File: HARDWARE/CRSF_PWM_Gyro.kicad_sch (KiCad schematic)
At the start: 3 parts, among them U1 STM32F103T8Ux, U2 TCR2EF33_LMCT

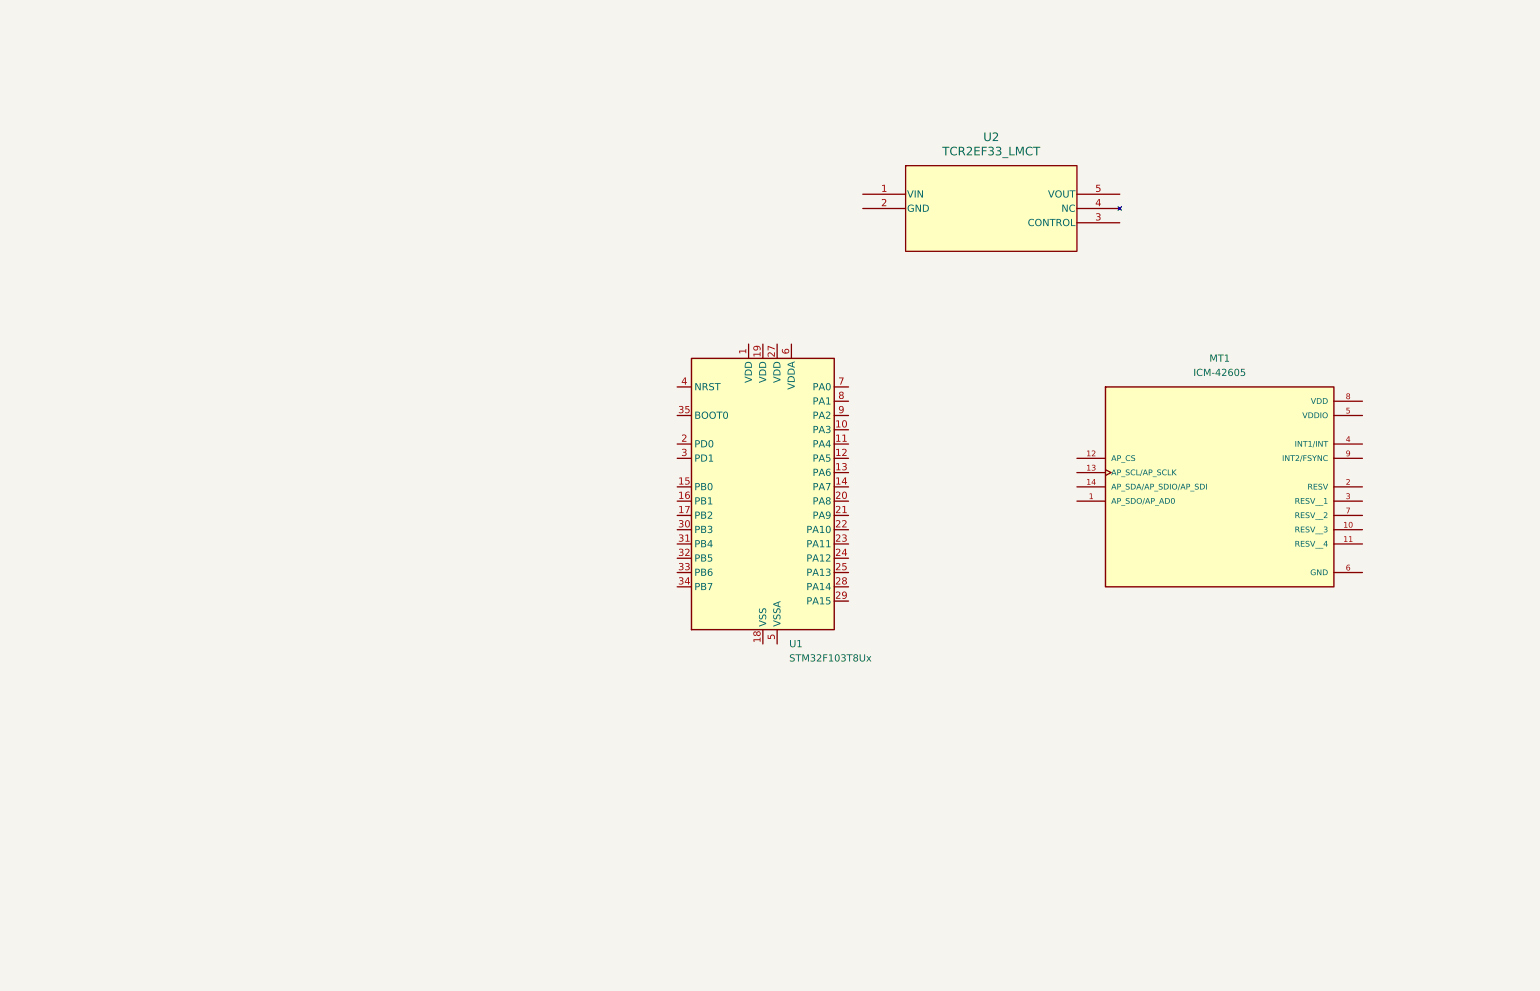
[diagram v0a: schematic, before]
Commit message: Pick different MCU and add USB C connector
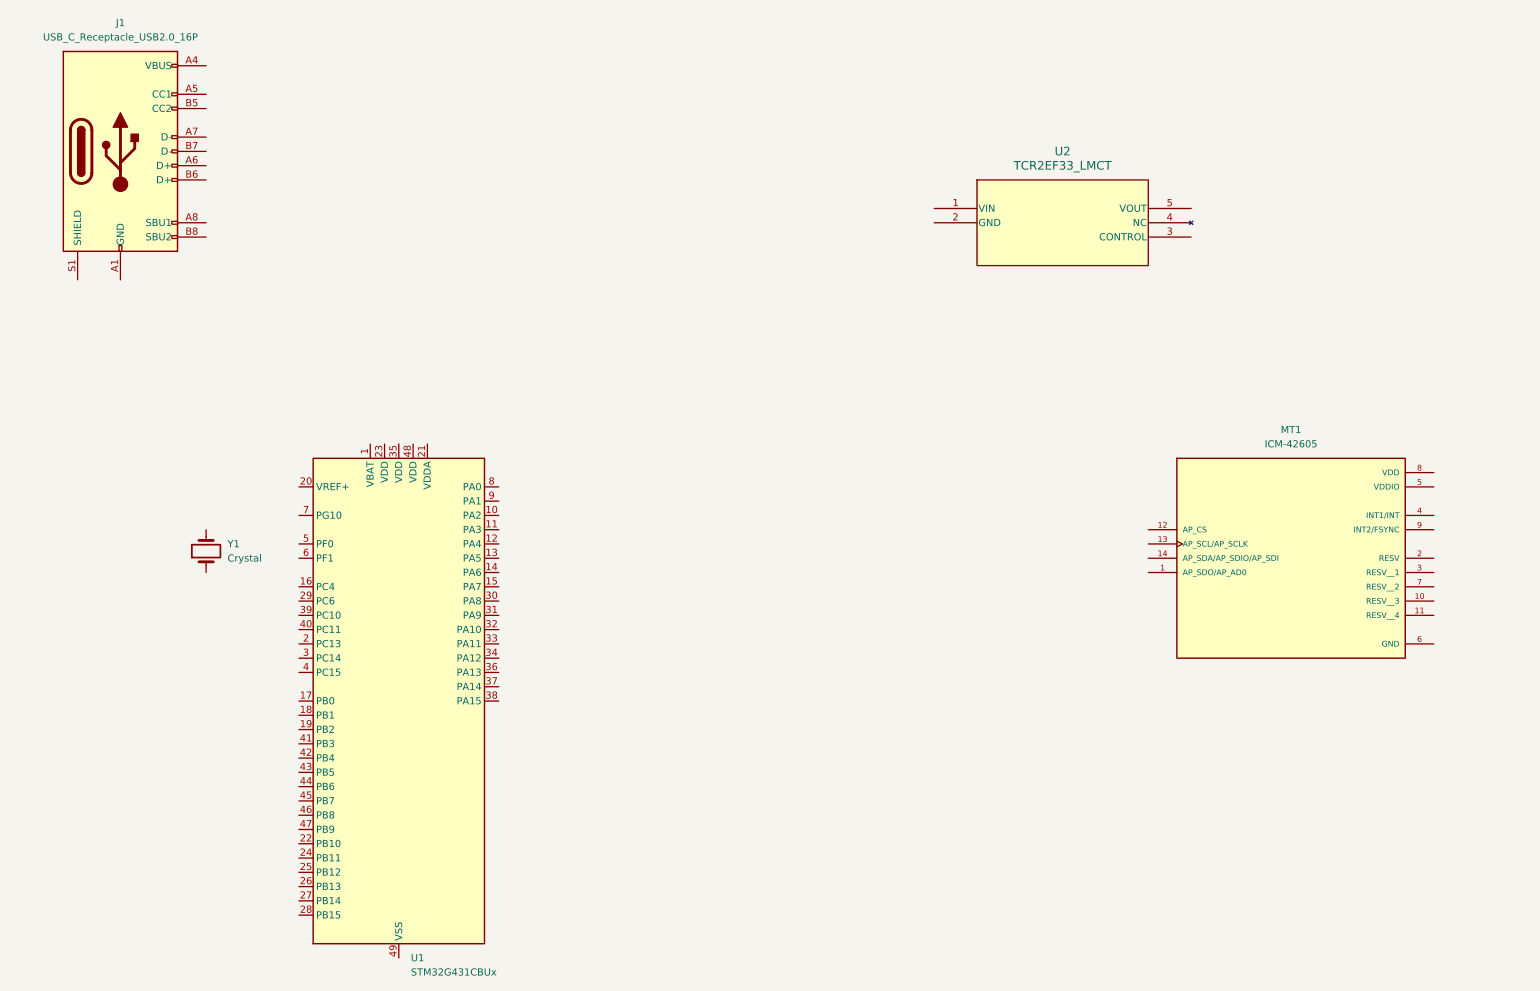
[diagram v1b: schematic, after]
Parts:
- removed U1: STM32F103T8Ux, Package_DFN_QFN:QFN-36-1EP_6x6mm_P0.5mm_EP4.1x4.1mm, symbol MCU_ST_STM32F1:STM32F103T8Ux
- added J1: USB_C_Receptacle_USB2.0_16P, symbol Connector:USB_C_Receptacle_USB2.0_16P
- added U1: STM32G431CBUx, Package_DFN_QFN:QFN-48-1EP_7x7mm_P0.5mm_EP5.6x5.6mm, symbol MCU_ST_STM32G4:STM32G431CBUx
- added Y1: Crystal, symbol Device:Crystal
- MT1: PN ICM-42605 -> (none); Part Number (none) -> 1428-1152-2-ND
- U2: PN TCR2EF33,LM(CT -> (none); Part Number (none) -> TCR2EF33LM(CTTR-ND
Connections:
- new net: J1.A1 (GND), J1.A12 (GND), J1.B1 (GND), J1.B12 (GND)
- new net: J1.A4 (VBUS), J1.A9 (VBUS), J1.B4 (VBUS), J1.B9 (VBUS)
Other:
- title: (none) -> CRSF_PWM_Gyro
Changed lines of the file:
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@@
 	(generator_version "9.0")
 	(paper "A4")
+	(title_block
+		(title "CRSF_PWM_Gyro")
+		(rev "v1.0")
+	)

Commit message: Add CRSF header and replace MCU with KB variant
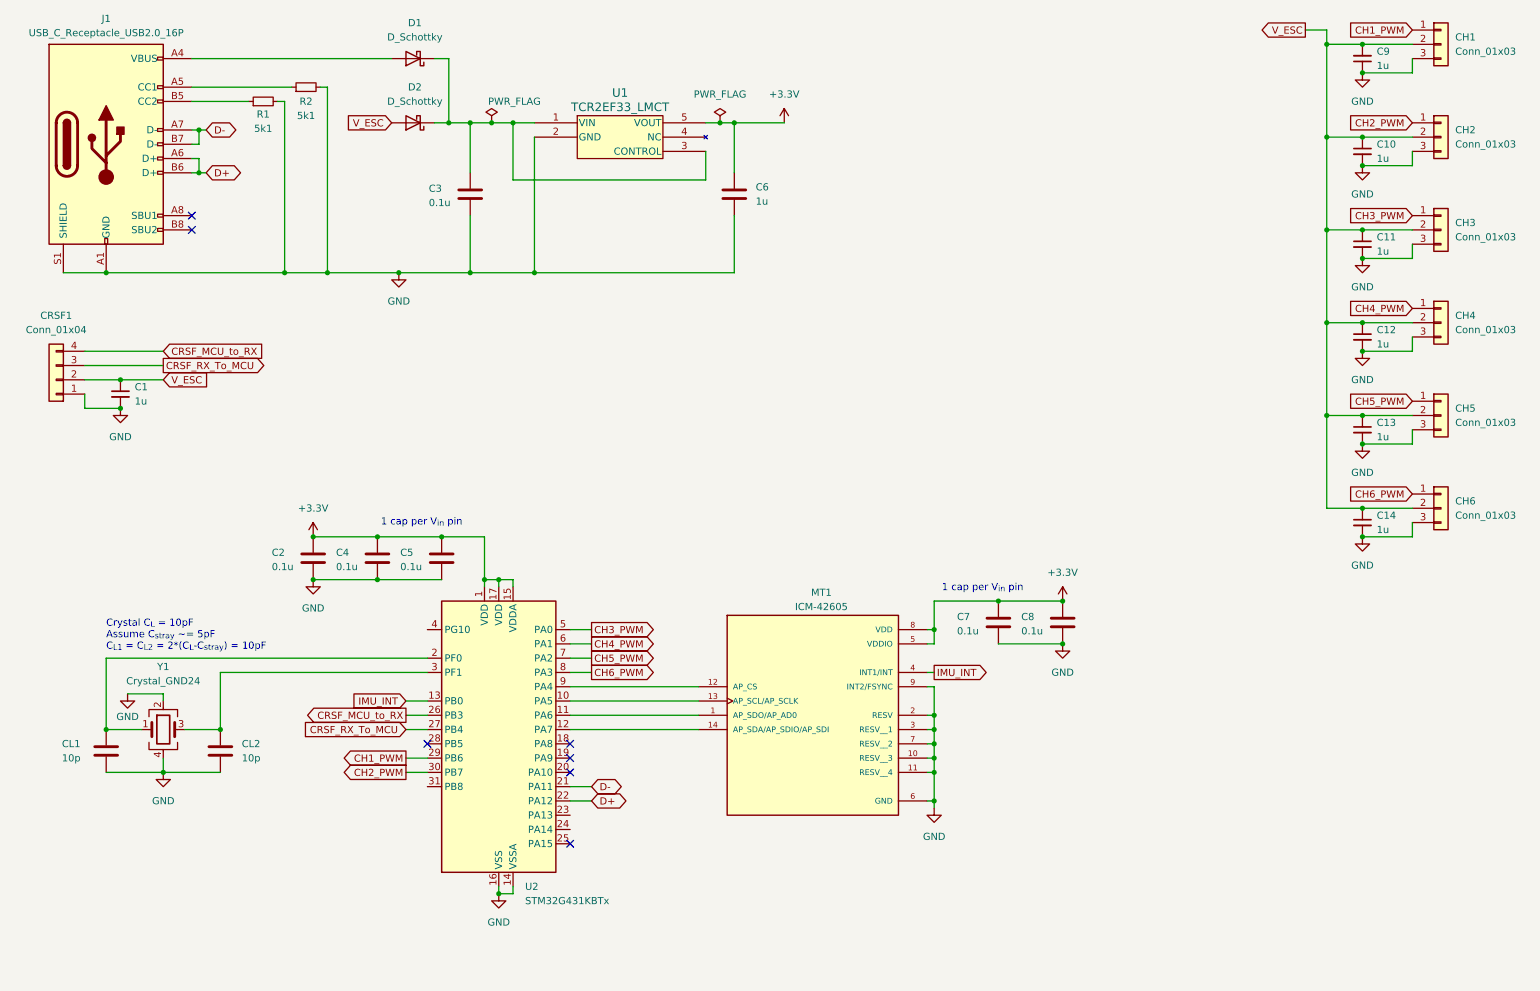
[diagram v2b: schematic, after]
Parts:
- removed U1: STM32G431CBUx, Package_DFN_QFN:QFN-48-1EP_7x7mm_P0.5mm_EP5.6x5.6mm, symbol MCU_ST_STM32G4:STM32G431CBUx
- removed Y1: Crystal, symbol Device:Crystal
- added C1, C10, C11, C12, C13, C14, C9: 1u, symbol Device:C_Small
- added C2, C3, C4, C5, C7, C8: 0.1u, symbol Device:C
- added C6: 1u, symbol Device:C
- added CH1, CH2, CH3, CH4, CH5, CH6: Conn_01x03, symbol Connector_Generic:Conn_01x03
- added CL1, CL2: 10p, symbol Device:C
- added CRSF1: Conn_01x04, symbol Connector_Generic:Conn_01x04
- added D1, D2: D_Schottky, symbol Device:D_Schottky
- added R1, R2: 5k1, symbol Device:R_Small
- added U2: STM32G431KBTx, Package_QFP:LQFP-32_7x7mm_P0.8mm, symbol MCU_ST_STM32G4:STM32G431KBTx
- added Y1: Crystal_GND24, symbol Device:Crystal_GND24
- J1: footprint (none) -> Connector_USB:USB_C_Receptacle_GCT_USB4105-xx-A_16P_TopMnt_Horizontal; Part Number 2073-USB4105-GF-ATR-ND -> (none)
- renumbered U2 to U1
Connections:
- net at MT1.1 (AP_SDO/AP_AD0): now also U2.11 (PA6)
- net GND: now reaches MT1.10 (RESV__3)
- net GND: now also J1.A1 (GND), J1.A12 (GND), J1.B1 (GND), J1.B12 (GND), J1.S1 (SHIELD), MT1.11 (RESV__4), MT1.2 (RESV), MT1.3 (RESV__1), MT1.6 (GND), MT1.7 (RESV__2), MT1.9 (INT2/FSYNC), U1.2 (GND), C1.2, C10.2, C11.2, C12.2, C13.2, C14.2, C2.2, C3.2, C4.2, C5.2, C6.2, C7.2, C8.2, C9.1, CH1.3 (Pin_3), CH2.3 (Pin_3), CH3.3 (Pin_3), CH4.3 (Pin_3), CH5.3 (Pin_3), CH6.3 (Pin_3), CL1.2, CL2.2, CRSF1.1 (Pin_1), R1.2, R2.2, U2.14 (VSSA), U2.16 (VSS), U2.32 (VSS), Y1.2, Y1.4
- net at MT1.12 (AP_CS): now also U2.9 (PA4)
- net at MT1.13 (AP_SCL/AP_SCLK): now also U2.10 (PA5)
- net at MT1.14 (AP_SDA/AP_SDIO/AP_SDI): now also U2.12 (PA7)
- net IMU_INT: now reaches MT1.4 (INT1/INT)
- net IMU_INT: now also U2.13 (PB0)
- net +3.3V: now reaches MT1.5 (VDDIO)
- net +3.3V: now also MT1.8 (VDD), U1.5 (VOUT), C2.1, C4.1, C5.1, C6.1, C7.1, C8.1, U2.1 (VDD), U2.15 (VDDA), U2.17 (VDD)
- net at U1.1 (VIN): now also U1.3 (CONTROL), C3.1, D1.1 (K), D2.1 (K)
- net at J1.A4 (VBUS), J1.A9 (VBUS), J1.B4 (VBUS)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: now also D1.2 (A)
- net at J1.A5 (CC1): now also R2.1
- net D+: now reaches J1.A6 (D+)
- net D+: now also J1.B6 (D+), U2.22 (PA12)
- net D-: now reaches J1.A7 (D-)
- net D-: now also J1.B7 (D-), U2.21 (PA11)
- net at J1.B5 (CC2): now also R1.1
- new net: CL1.1, U2.2 (PF0), Y1.1
- new net: CL2.1, U2.3 (PF1), Y1.3
- new net CH1_PWM: CH1.1 (Pin_1), U2.29 (PB6)
- new net CH2_PWM: CH2.1 (Pin_1), U2.30 (PB7)
- new net CH3_PWM: CH3.1 (Pin_1), U2.5 (PA0)
- new net CH4_PWM: CH4.1 (Pin_1), U2.6 (PA1)
- new net CH5_PWM: CH5.1 (Pin_1), U2.7 (PA2)
- new net CH6_PWM: CH6.1 (Pin_1), U2.8 (PA3)
- new net CRSF_MCU_to_RX: CRSF1.4 (Pin_4), U2.26 (PB3)
- new net CRSF_RX_To_MCU: CRSF1.3 (Pin_3), U2.27 (PB4)
- new net V_ESC: C1.1, C10.1, C11.1, C12.1, C13.1, C14.1, C9.2, CH1.2 (Pin_2), CH2.2 (Pin_2), CH3.2 (Pin_2), CH4.2 (Pin_2), CH5.2 (Pin_2), CH6.2 (Pin_2), CRSF1.2 (Pin_2), D2.2 (A)
- no-connect marks 0 -> 7
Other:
- note added: "1 cap per V_{in} pin"
- note added: "Crystal C_{L} = 10pF Assume C_{stray} ~= 5pF C_{L1} = C_{L2} = 2*(C_{L}-C_{stray}) = 10pF"
- moved on the sheet: MT1, U1

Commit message: Separate schematic into pages
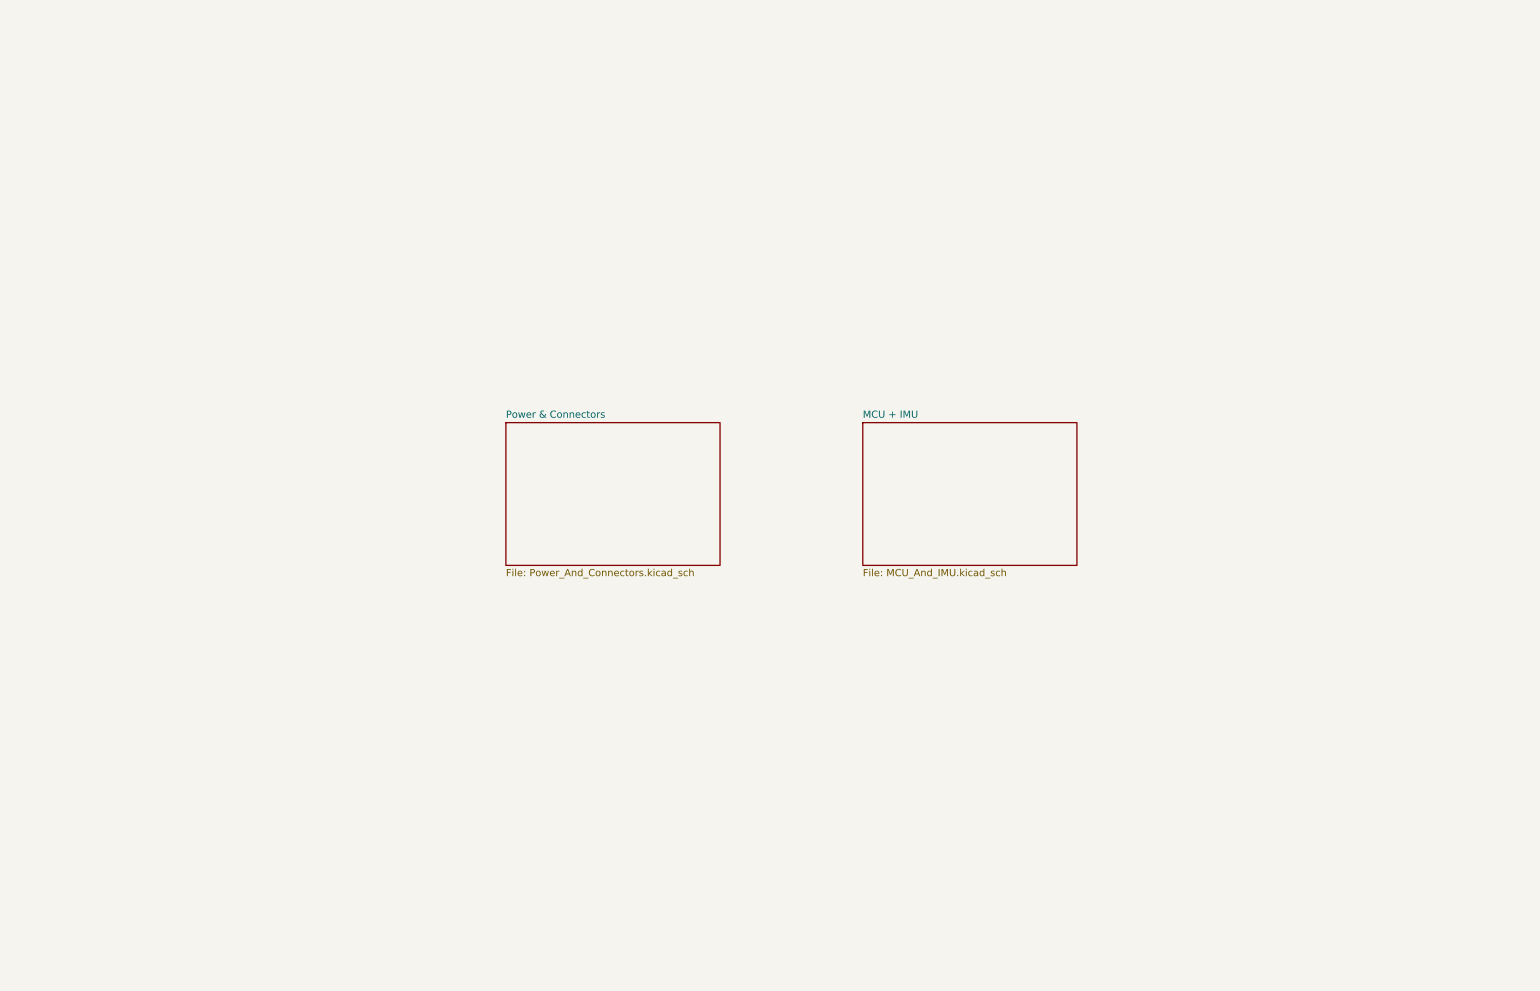
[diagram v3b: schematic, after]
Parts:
- removed C1, C10, C11, C12, C13, C14, C9: 1u, symbol Device:C_Small
- removed C2, C3, C4, C5, C7, C8: 0.1u, symbol Device:C
- removed C6: 1u, symbol Device:C
- removed CH1, CH2, CH3, CH4, CH5, CH6: Conn_01x03, symbol Connector_Generic:Conn_01x03
- removed CL1, CL2: 10p, symbol Device:C
- removed CRSF1: Conn_01x04, symbol Connector_Generic:Conn_01x04
- removed D1, D2: D_Schottky, symbol Device:D_Schottky
- removed J1: USB_C_Receptacle_USB2.0_16P, Connector_USB:USB_C_Receptacle_GCT_USB4105-xx-A_16P_TopMnt_Horizontal, symbol Connector:USB_C_Receptacle_USB2.0_16P
- removed MT1: ICM-42605, Package_LGA_Custom:XDCR_ICM-42605, symbol Sensor_Motion_Custom:ICM-42605
- removed R1, R2: 5k1, symbol Device:R_Small
- removed U1: TCR2EF33_LMCT, Package_TO_SOT_SMD_Custom:SOT-25 SMV_TOS, symbol Regulator_Linear_Custom:TCR2EF33_LMCT
- removed U2: STM32G431KBTx, Package_QFP:LQFP-32_7x7mm_P0.8mm, symbol MCU_ST_STM32G4:STM32G431KBTx
- removed Y1: Crystal_GND24, symbol Device:Crystal_GND24
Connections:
- no-connect marks 7 -> 0
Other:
- added sheet MCU + IMU (MCU_And_IMU.kicad_sch)
- added sheet Power & Connectors (Power_And_Connectors.kicad_sch)
- note removed: "1 cap per V_{in} pin"
- note removed: "Crystal C_{L} = 10pF Assume C_{stray} ~= 5pF C_{L1} = C_{L2} = 2*(C_{L}-C_{stray}) = 10pF"
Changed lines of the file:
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@@
 		(rev "v1.0")
 	)
+	(sheet
+		(at 101.6 88.9)
+		(size 38.1 25.4)
+		(exclude_from_sim no)
+		(in_bom yes)
+		(on_board yes)
+		(dnp no)
+		(fields_autoplaced yes)
+		(stroke
+			(width 0.1524)
+			(type solid)
+		)
+		(fill
+			(color 0 0 0 0.0000)
+		)
+		(property "Sheetname" "Power & Connectors"
+			(at 101.6 88.1884 0)
+			(effects
+				(font
+					(size 1.27 1.27)
+				)
+				(justify left bottom)
+			)
+		)
+		(property "Sheetfile" "Power_And_Connectors.kicad_sch"
+			(at 101.6 114.8846 0)
+			(effects
+				(font
+					(size 1.27 1.27)
+				)
+				(justify left top)
+			)
+		)
+		(instances
+			(project "CRSF_PWM_Gyro"
+				(path "/01c12cb5-5cfe-484a-838c-9cbfa05ce5f4"
+					(page "2")
+				)
+			)
+		)
+	)
+	(sheet
+		(at 165.1 88.9)
+		(size 38.1 25.4)
+		(exclude_from_sim no)
+		(in_bom yes)
+		(on_board yes)
+		(dnp no)
+		(fields_autoplaced yes)
+		(stroke
+			(width 0.1524)
+			(type solid)
+		)
+		(fill
+			(color 0 0 0 0.0000)
+		)
+		(property "Sheetname" "MCU + IMU"
+			(at 165.1 88.1884 0)
+			(effects
+				(font
+					(size 1.27 1.27)
+				)
+				(justify left bottom)
+			)
+		)
+		(property "Sheetfile" "MCU_And_IMU.kicad_sch"
+			(at 165.1 114.8846 0)
+			(effects
+				(font
+					(size 1.27 1.27)
+				)
+				(justify left top)
+			)
+		)
+		(instances
+			(project "CRSF_PWM_Gyro"
+				(path "/01c12cb5-5cfe-484a-838c-9cbfa05ce5f4"
+					(page "3")
+				)
+			)
+		)
+	)
+	(sheet_instances
+		(path "/"
+			(page "1")
+		)
+	)
+	(embedded_fonts no)
+)

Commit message: Update footprints and add all PNs
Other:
- sheet Power & Connectors renamed Power + Connectors
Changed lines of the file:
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@@
 			(color 0 0 0 0.0000)
 		)
-		(property "Sheetname" "Power & Connectors"
+		(property "Sheetname" "Power + Connectors"
 			(at 101.6 88.1884 0)
 			(effects
